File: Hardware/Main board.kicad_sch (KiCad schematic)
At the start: 39 parts, among them J1 RBUS, U1 ESP32-S3, Y1 R940000171

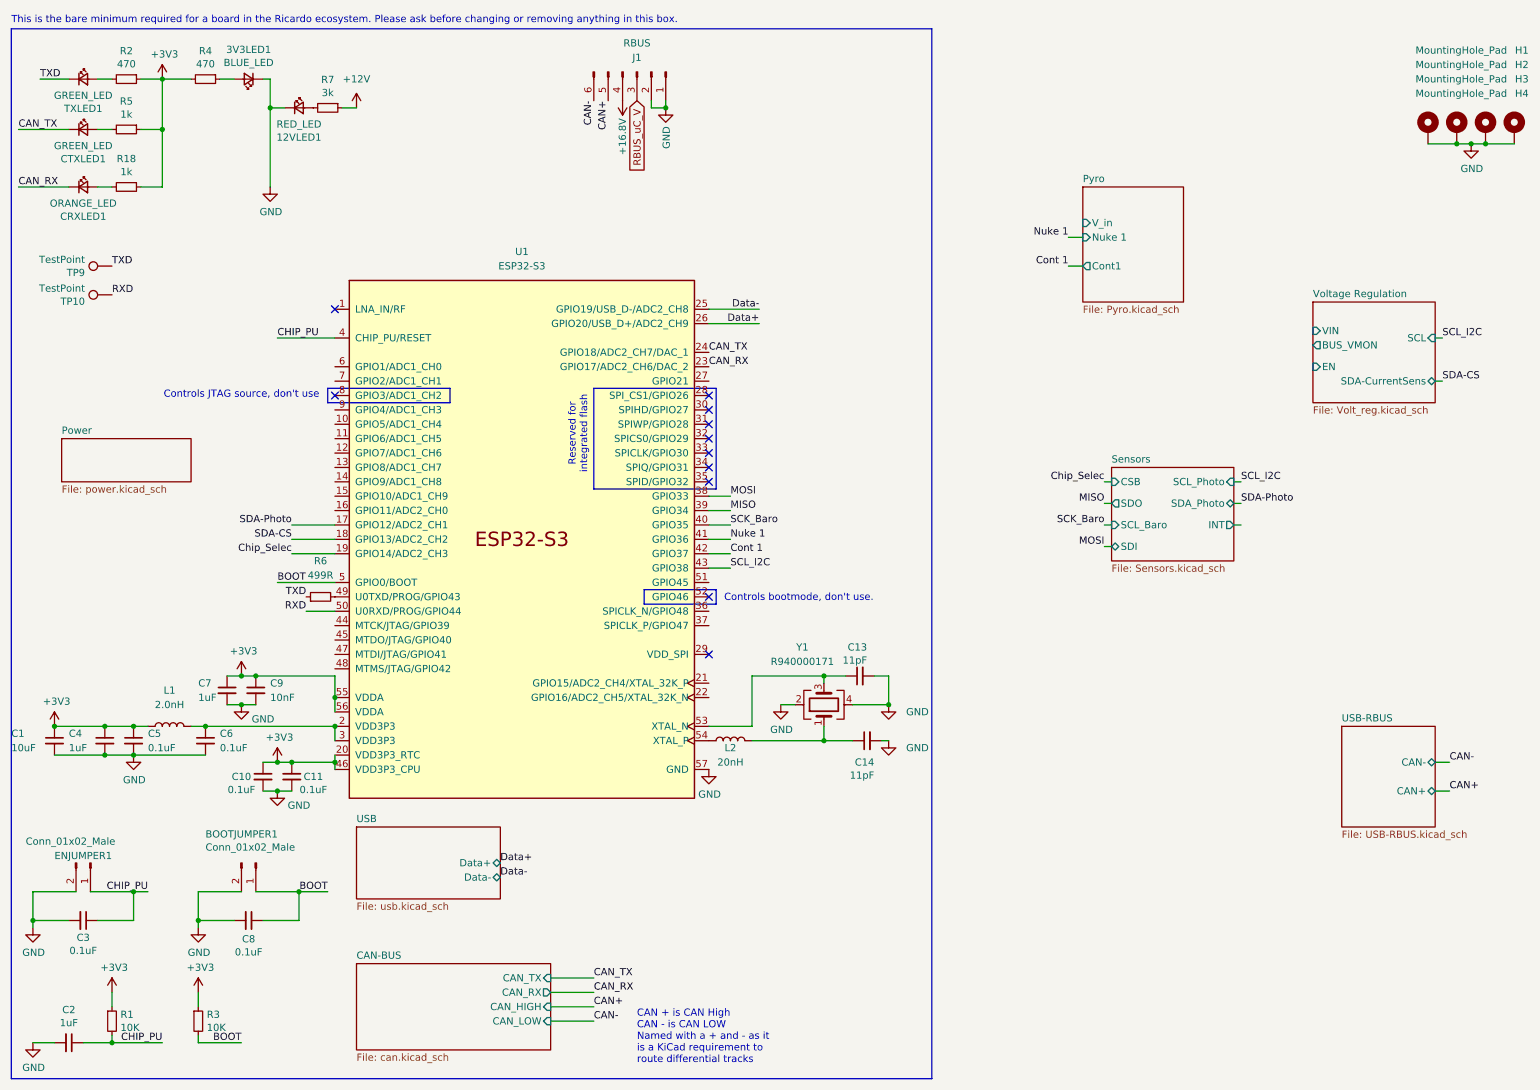
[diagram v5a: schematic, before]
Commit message: Voltage regulation done + used photo ic sensor library
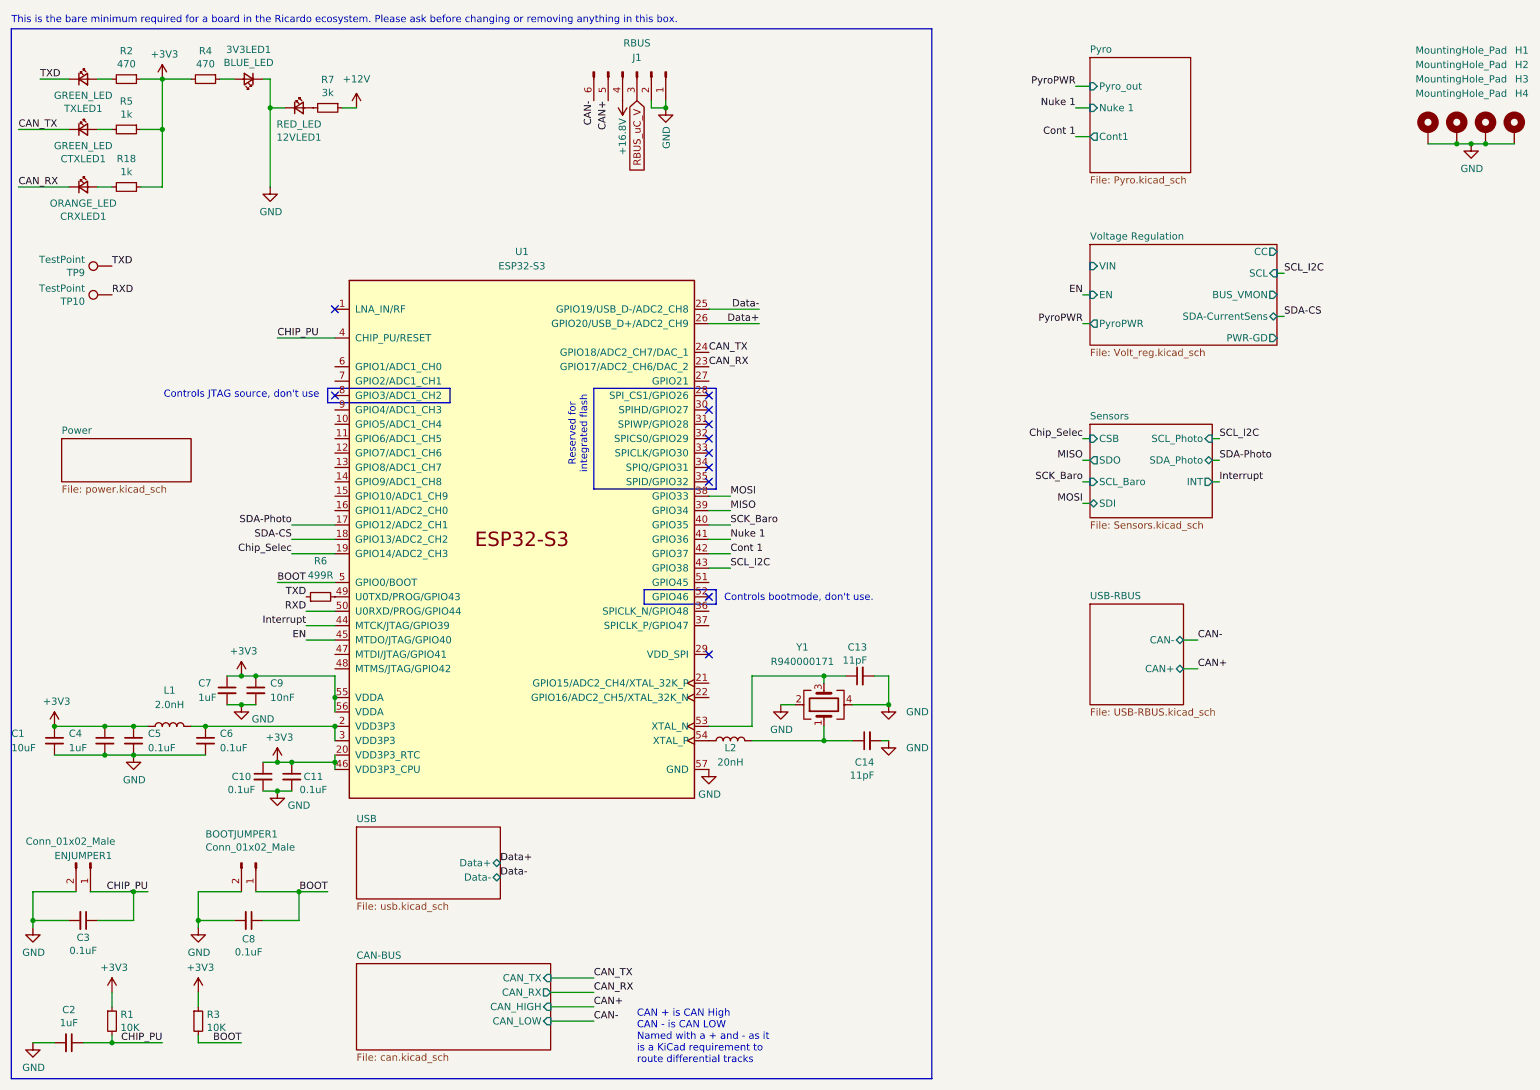
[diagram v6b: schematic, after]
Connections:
- net Interrupt : now reaches U1.44 (MTCK/JTAG/GPIO39)
- net EN: now reaches U1.45 (MTDO/JTAG/GPIO40)
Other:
- sheet Pyro ports: added Pyro_out; removed V_in
- sheet Voltage Regulation ports: added CC, PWR-GD, PyroPWR; removed none
